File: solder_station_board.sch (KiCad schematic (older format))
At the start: 40 parts, among them J1 PWR_5_36, J3 RT_WELLER, J5 INPUT, J6 PWR_15V, J8 SERIAL, J9 INPUT, P1 ISP, Q1 IRF9540, Q2 2N7002, U4 TLC272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

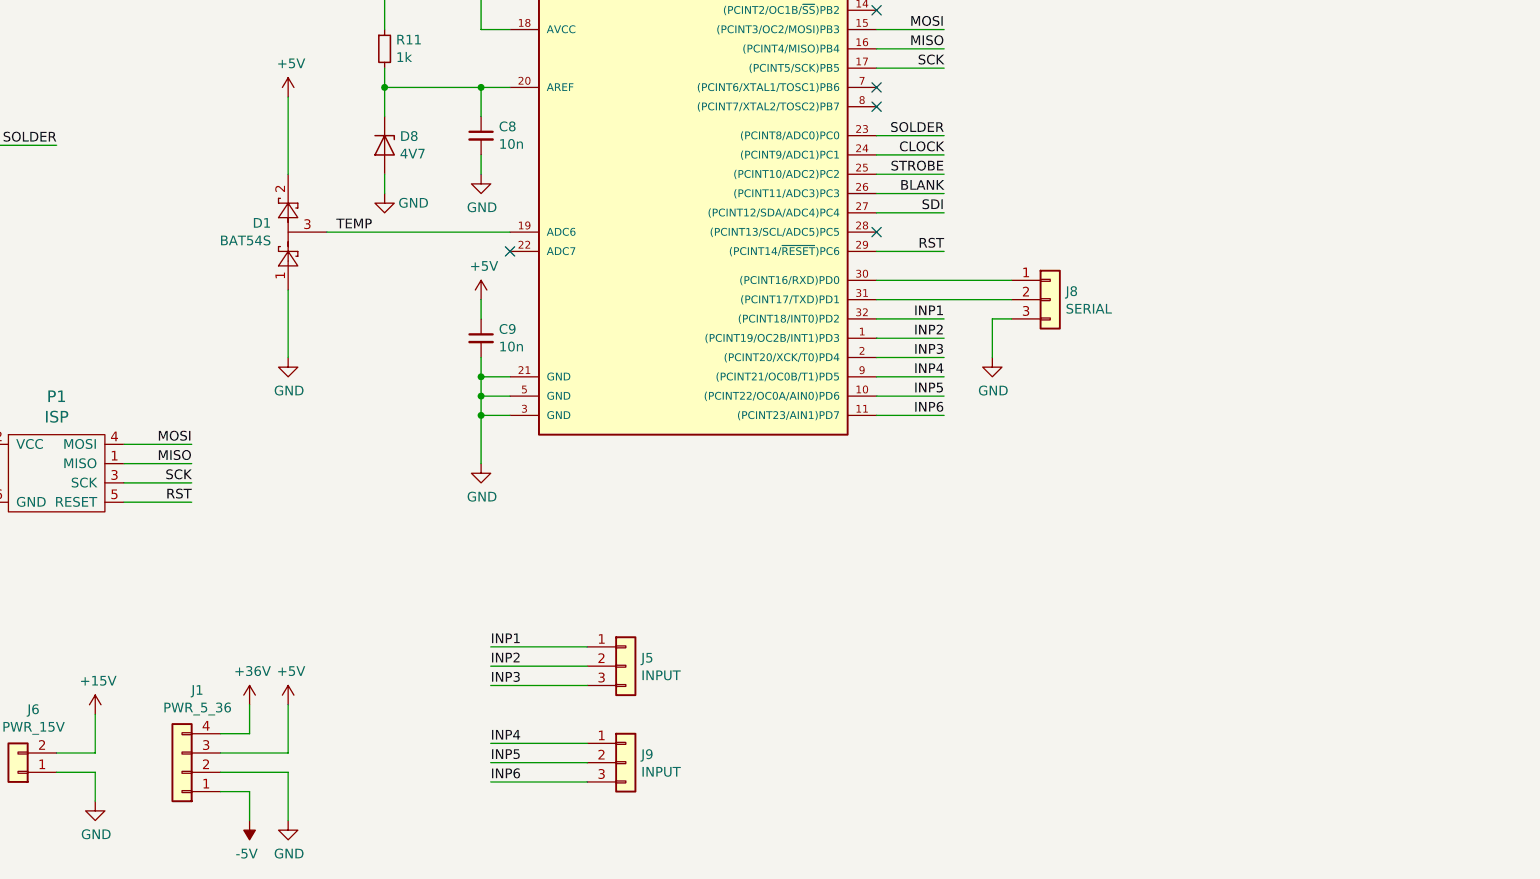
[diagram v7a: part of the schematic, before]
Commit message: new board just the adc, atmega and the pnp transistor.
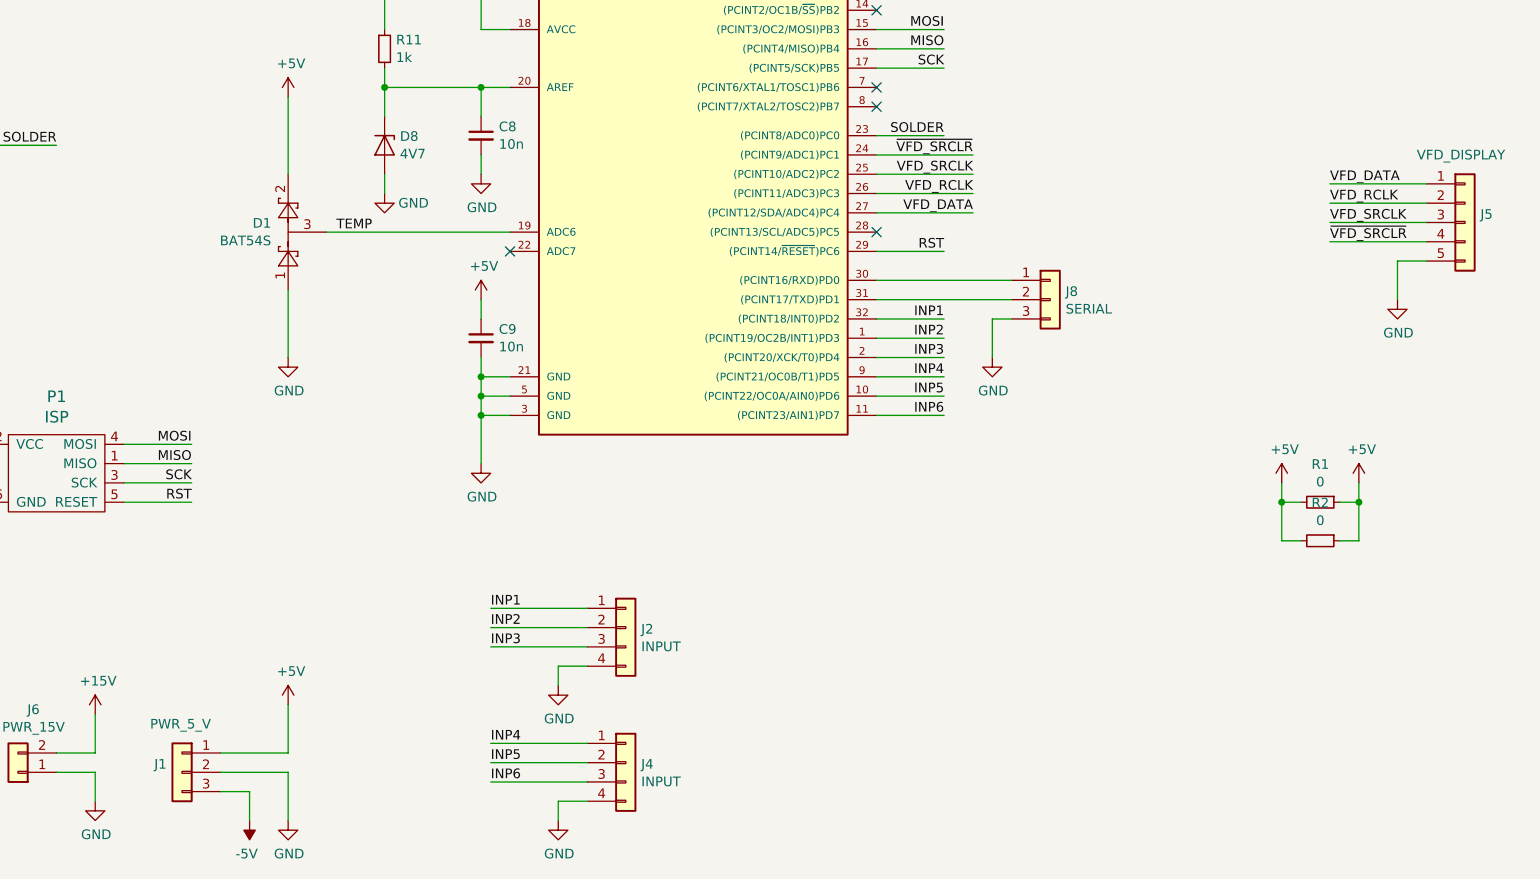
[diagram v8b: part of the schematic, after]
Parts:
- removed J1: PWR_5_36, Connector_PinHeader_2.54mm:PinHeader_1x04_P2.54mm_Vertical, symbol Connector_Generic:Conn_01x04
- removed J5, J9: INPUT, Connector_PinSocket_2.54mm:PinSocket_1x03_P2.54mm_Vertical, symbol Connector_Generic:Conn_01x03
- added J1: PWR_5_V, Connector_PinSocket_2.54mm:PinSocket_1x03_P2.54mm_Vertical, symbol Connector_Generic:Conn_01x03
- added J2, J4: INPUT, Connector_PinHeader_2.54mm:PinHeader_1x04_P2.54mm_Vertical, symbol Connector_Generic:Conn_01x04
- added J5: VFD_DISPLAY, Connector_PinHeader_2.54mm:PinHeader_1x05_P2.54mm_Vertical, symbol Connector_Generic:Conn_01x05
- added R1, R2: 0, Resistor_SMD:R_1206_3216Metric, symbol Device:R_Small
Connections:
- net +5V: now also J1.1 (Pin_1), R1.1, R1.2, R2.1, R2.2
- net -5V: now also J1.3 (Pin_3)
- net GND: now also J1.2 (Pin_2), J2.4 (Pin_4), J4.4 (Pin_4), J5.5 (Pin_5)
- net INP1: now also J2.1 (Pin_1)
- net INP2: now also J2.2 (Pin_2)
- net INP3: now also J2.3 (Pin_3)
- net INP4: now also J4.1 (Pin_1)
- net INP5: now also J4.2 (Pin_2)
- net INP6: now also J4.3 (Pin_3)
- net BLANK renamed VFD_RCLK
- net VFD_RCLK: now also J5.2 (Pin_2)
- net CLOCK renamed ~VFD_SRCLR
- net ~VFD_SRCLR: now also J5.4 (Pin_4)
- net SDI renamed VFD_DATA
- net VFD_DATA: now also J5.1 (Pin_1)
- net STROBE renamed VFD_SRCLK
- net VFD_SRCLK: now also J5.3 (Pin_3)
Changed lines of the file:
@@
 Wire Wire Line
 	850  6050 850  6250
-Wire Wire Line
-	6900 4100 6550 4100
-Text Label 6900 4400 2    50   ~ 0
-SDI
-Text Label 6900 4300 2    50   ~ 0
-BLANK
-Wire Wire Line
-	6900 4400 6550 4400
-Text Label 6900 4200 2    50   ~ 0
-STROBE
-Wire Wire Line
-	6900 4300 6550 4300
-Text Label 6900 4100 2    50   ~ 0
-CLOCK
-Wire Wire Line
-	6900 4200 6550 4200
+Text Label 7050 4400 2    50   ~ 0
+VFD_DATA
+Text Label 7050 4100 2    50   ~ 0
+~VFD_SRCLR
+Text Label 7050 4200 2    50   ~ 0
+VFD_SRCLK
+Text Label 7050 4300 2    50   ~ 0
+VFD_RCLK
 Wire Wire Line
 	4500 4200 4500 4100
@@
 $EndComp
 $Comp
-L Connector_Generic:Conn_01x04 J1
-U 1 1 5B600371
-P 2950 7300
-F 0 "J1" H 2870 6875 50  0000 C CNN
-F 1 "PWR_5_36" H 2870 6966 50  0000 C CNN
-F 2 "Connector_PinHeader_2.54mm:PinHeader_1x04_P2.54mm_Vertical" H 2950 7300 50  0001 C CNN
-F 3 "~" H 2950 7300 50  0001 C CNN
-	1    2950 7300
-	-1   0    0    1
-$EndComp
-$Comp
-L power:+36V #PWR0102
-U 1 1 5B60076A
-P 3300 6950
-F 0 "#PWR0102" H 3300 6800 50  0001 C CNN
-F 1 "+36V" H 3315 7123 50  0000 C CNN
-F 2 "" H 3300 6950 50  0001 C CNN
-F 3 "" H 3300 6950 50  0001 C CNN
-	1    3300 6950
-	1    0    0    -1
-$EndComp
-Wire Wire Line
-	3300 6950 3300 7100
-Wire Wire Line
-	3300 7100 3150 7100
-$Comp
 L power:+5V #PWR0103
 U 1 1 5B608E3E
@@
 L power:GND #PWR0130
 U 1 1 5BC5EEC9
-P 7150 5150
-F 0 "#PWR0130" H 7150 4900 50  0001 C CNN
-F 1 "GND" H 7155 4977 50  0000 C CNN
-F 2 "" H 7150 5150 50  0001 C CNN
-F 3 "" H 7150 5150 50  0001 C CNN
-	1    7150 5150
-	1    0    0    -1
-$EndComp
-Wire Wire Line
-	7150 5150 7150 4950
+P 9250 4850
+F 0 "#PWR0130" H 9250 4600 50  0001 C CNN
+F 1 "GND" H 9255 4677 50  0000 C CNN
+F 2 "" H 9250 4850 50  0001 C CNN
+F 3 "" H 9250 4850 50  0001 C CNN
+	1    9250 4850
+	1    0    0    -1
+$EndComp
+Wire Wire Line
+	9250 4850 9250 4650
 Wire Wire Line
 	7150 4950 7250 4950
@@
 Wire Wire Line
 	6550 4750 7250 4750
-$Comp
-L Connector_Generic:Conn_01x03 J5
-U 1 1 5BC945DB
-P 5250 6750
-F 0 "J5" H 5330 6792 50  0000 L CNN
-F 1 "INPUT" H 5330 6701 50  0000 L CNN
-F 2 "Connector_PinSocket_2.54mm:PinSocket_1x03_P2.54mm_Vertical" H 5250 6750 50  0001 C CNN
-F 3 "~" H 5250 6750 50  0001 C CNN
-	1    5250 6750
-	1    0    0    -1
-$EndComp
 Wire Wire Line
 	6550 4950 6900 4950
@@
 Text Label 6900 5150 2    50   ~ 0
 INP3
+Text Label 4550 6450 0    50   ~ 0
+INP1
+Text Label 4550 6550 0    50   ~ 0
+INP2
 Text Label 4550 6650 0    50   ~ 0
-INP1
-Text Label 4550 6750 0    50   ~ 0
-INP2
-Text Label 4550 6850 0    50   ~ 0
 INP3
 Wire Wire Line
-	4550 6750 5050 6750
+	4550 6550 5050 6550
+Wire Wire Line
+	4550 6450 5050 6450
 Wire Wire Line
 	4550 6650 5050 6650
-Wire Wire Line
-	4550 6850 5050 6850
 Wire Wire Line
 	6550 5250 6900 5250
@@
 Text Label 6900 5450 2    50   ~ 0
 INP6
-$Comp
-L Connector_Generic:Conn_01x03 J9
-U 1 1 5BF5FFB0
-P 5250 7250
-F 0 "J9" H 5330 7292 50  0000 L CNN
-F 1 "INPUT" H 5330 7201 50  0000 L CNN
-F 2 "Connector_PinSocket_2.54mm:PinSocket_1x03_P2.54mm_Vertical" H 5250 7250 50  0001 C CNN
-F 3 "~" H 5250 7250 50  0001 C CNN
-	1    5250 7250
-	1    0    0    -1
-$EndComp
 Text Label 4550 7150 0    50   ~ 0
 INP4
@@
 Wire Wire Line
 	4200 1600 4200 1800
+$Comp
+L Connector_Generic:Conn_01x03 J1
+U 1 1 5CAFBF53
+P 2950 7300
+F 0 "J1" H 3030 7342 50  0000 L CNN
+F 1 "PWR_5_V" H 2800 7550 50  0000 L CNN
+F 2 "Connector_PinSocket_2.54mm:PinSocket_1x03_P2.54mm_Vertical" H 2950 7300 50  0001 C CNN
+F 3 "~" H 2950 7300 50  0001 C CNN
+	1    2950 7300
+	-1   0    0    -1
+$EndComp
+Wire Wire Line
+	6550 4400 7050 4400
+Wire Wire Line
+	6550 4100 7050 4100
+Wire Wire Line
+	6550 4200 7050 4200
+Wire Wire Line
+	6550 4300 7050 4300
+Text Label 8900 4250 0    50   ~ 0
+VFD_DATA
+Text Label 8900 4550 0    50   ~ 0
+~VFD_SRCLR
+Text Label 8900 4450 0    50   ~ 0
+VFD_SRCLK
+Text Label 8900 4350 0    50   ~ 0
+VFD_RCLK
+Wire Wire Line
+	9400 4250 8900 4250
+Wire Wire Line
+	9400 4550 8900 4550
+Wire Wire Line
+	9400 4450 8900 4450
+Wire Wire Line
+	9400 4350 8900 4350
+$Comp
+L Connector_Generic:Conn_01x05 J5
+U 1 1 5CB2243C
+P 9600 4450
+F 0 "J5" H 9680 4492 50  0000 L CNN
+F 1 "VFD_DISPLAY" H 9350 4800 50  0000 L CNN
+F 2 "Connector_PinHeader_2.54mm:PinHeader_1x05_P2.54mm_Vertical" H 9600 4450 50  0001 C CNN
+F 3 "~" H 9600 4450 50  0001 C CNN
+	1    9600 4450
+	1    0    0    -1
+$EndComp
+Wire Wire Line
+	9250 4650 9400 4650
+$Comp
+L power:GND #PWR03
+U 1 1 5CB3758A
+P 7150 5150
+F 0 "#PWR03" H 7150 4900 50  0001 C CNN
+F 1 "GND" H 7155 4977 50  0000 C CNN
+F 2 "" H 7150 5150 50  0001 C CNN
+F 3 "" H 7150 5150 50  0001 C CNN
+	1    7150 5150
+	1    0    0    -1
+$EndComp
+Wire Wire Line
+	7150 5150 7150 4950
+$Comp
+L Connector_Generic:Conn_01x04 J2
+U 1 1 5CB42664
+P 5250 6550
+F 0 "J2" H 5330 6542 50  0000 L CNN
+F 1 "INPUT" H 5330 6451 50  0000 L CNN
+F 2 "Connector_PinHeader_2.54mm:PinHeader_1x04_P2.54mm_Vertical" H 5250 6550 50  0001 C CNN
+F 3 "~" H 5250 6550 50  0001 C CNN
+	1    5250 6550
+	1    0    0    -1
+$EndComp
+$Comp
+L power:GND #PWR01
+U 1 1 5CB4296F
+P 4900 6850
+F 0 "#PWR01" H 4900 6600 50  0001 C CNN
+F 1 "GND" H 4905 6677 50  0000 C CNN
+F 2 "" H 4900 6850 50  0001 C CNN
+F 3 "" H 4900 6850 50  0001 C CNN
+	1    4900 6850
+	1    0    0    -1
+$EndComp
+Wire Wire Line
+	4900 6850 4900 6750
+Wire Wire Line
+	4900 6750 5050 6750
+$Comp
+L power:GND #PWR02
+U 1 1 5CB4D84E
+P 4900 7550
+F 0 "#PWR02" H 4900 7300 50  0001 C CNN
+F 1 "GND" H 4905 7377 50  0000 C CNN
+F 2 "" H 4900 7550 50  0001 C CNN
+F 3 "" H 4900 7550 50  0001 C CNN
+	1    4900 7550
+	1    0    0    -1
+$EndComp
+Wire Wire Line
+	4900 7550 4900 7450
+Wire Wire Line
+	4900 7450 5050 7450
+$Comp
+L Connector_Generic:Conn_01x04 J4
+U 1 1 5CB59179
+P 5250 7250
+F 0 "J4" H 5330 7242 50  0000 L CNN
+F 1 "INPUT" H 5330 7151 50  0000 L CNN
+F 2 "Connector_PinHeader_2.54mm:PinHeader_1x04_P2.54mm_Vertical" H 5250 7250 50  0001 C CNN
+F 3 "~" H 5250 7250 50  0001 C CNN
+	1    5250 7250
+	1    0    0    -1
+$EndComp
+$Comp
+L power:+5V #PWR04
+U 1 1 5CB070E5
+P 8650 5800
+F 0 "#PWR04" H 8650 5650 50  0001 C CNN
+F 1 "+5V" H 8665 5973 50  0000 C CNN
+F 2 "" H 8650 5800 50  0001 C CNN
+F 3 "" H 8650 5800 50  0001 C CNN
+	1    8650 5800
+	1    0    0    -1
+$EndComp
+$Comp
+L Device:R_Small R1
+U 1 1 5CB07375
+P 8850 5900
+F 0 "R1" V 8654 5900 50  0000 C CNN
+F 1 "0" V 8745 5900 50  0000 C CNN
+F 2 "Resistor_SMD:R_1206_3216Metric" H 8850 5900 50  0001 C CNN
+F 3 "~" H 8850 5900 50  0001 C CNN
+	1    8850 5900
+	0    1    1    0
+$EndComp
+$Comp
+L power:+5V #PWR05
+U 1 1 5CB074F4
+P 9050 5800
+F 0 "#PWR05" H 9050 5650 50  0001 C CNN
+F 1 "+5V" H 9065 5973 50  0000 C CNN
+F 2 "" H 9050 5800 50  0001 C CNN
+F 3 "" H 9050 5800 50  0001 C CNN
+	1    9050 5800
+	1    0    0    -1
+$EndComp
+Wire Wire Line
+	9050 5800 9050 5900
+Wire Wire Line
+	9050 5900 8950 5900
+Wire Wire Line
+	8750 5900 8650 5900
+Wire Wire Line
+	8650 5900 8650 5800
+$Comp
+L Device:R_Small R2
+U 1 1 5CB13331
+P 8850 6100
+F 0 "R2" V 8654 6100 50  0000 C CNN
+F 1 "0" V 8745 6100 50  0000 C CNN
+F 2 "Resistor_SMD:R_1206_3216Metric" H 8850 6100 50  0001 C CNN
+F 3 "~" H 8850 6100 50  0001 C CNN
+	1    8850 6100
+	0    1    1    0
+$EndComp
+Wire Wire Line
+	8950 6100 9050 6100
+Wire Wire Line
+	9050 6100 9050 5900
+Connection ~ 9050 5900
+Wire Wire Line
+	8650 5900 8650 6100
+Wire Wire Line
+	8650 6100 8750 6100
+Connection ~ 8650 5900
 $EndSCHEMATC
